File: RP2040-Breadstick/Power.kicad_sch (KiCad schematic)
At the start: 19 parts, among them J501 Conn_01x01, J502 Conn_01x01, J503 Conn_01x01, J504 Conn_01x01, J505 Conn_01x01, J506 Conn_01x01, J507 Conn_01x01, J508 Conn_01x01, J509 Conn_01x01, J510 Conn_01x01, U501 MIC5528-3.3YMT-TR

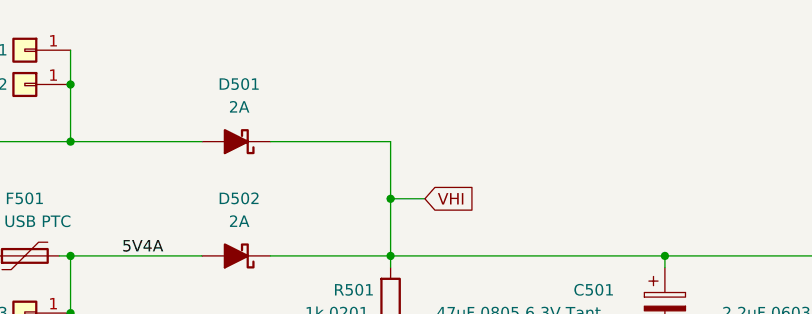
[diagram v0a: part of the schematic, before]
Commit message: Added a note about adding ideal ORing diodes IC
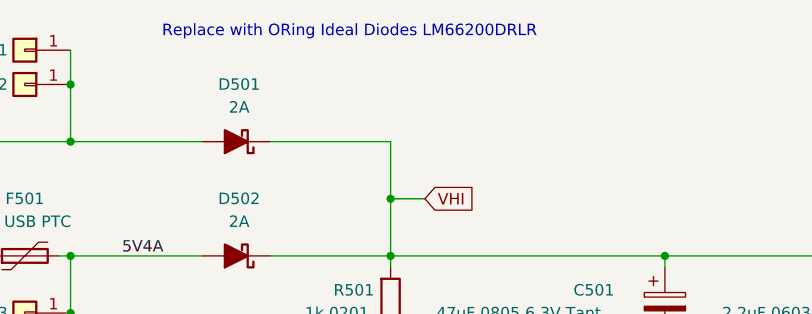
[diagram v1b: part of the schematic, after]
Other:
- note added: "Replace with ORing Ideal Diodes LM66200DRLR"
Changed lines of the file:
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@@
     (stroke (width 0) (type default) (color 0 0 0 0))
+  )
+  (text "Replace with ORing Ideal Diodes LM66200DRLR" (at 74.93 52.07 0)
+    (effects (font (size 1.27 1.27)) (justify left bottom))
   )
   (label "5V4A" (at 70.485 76.2 0)

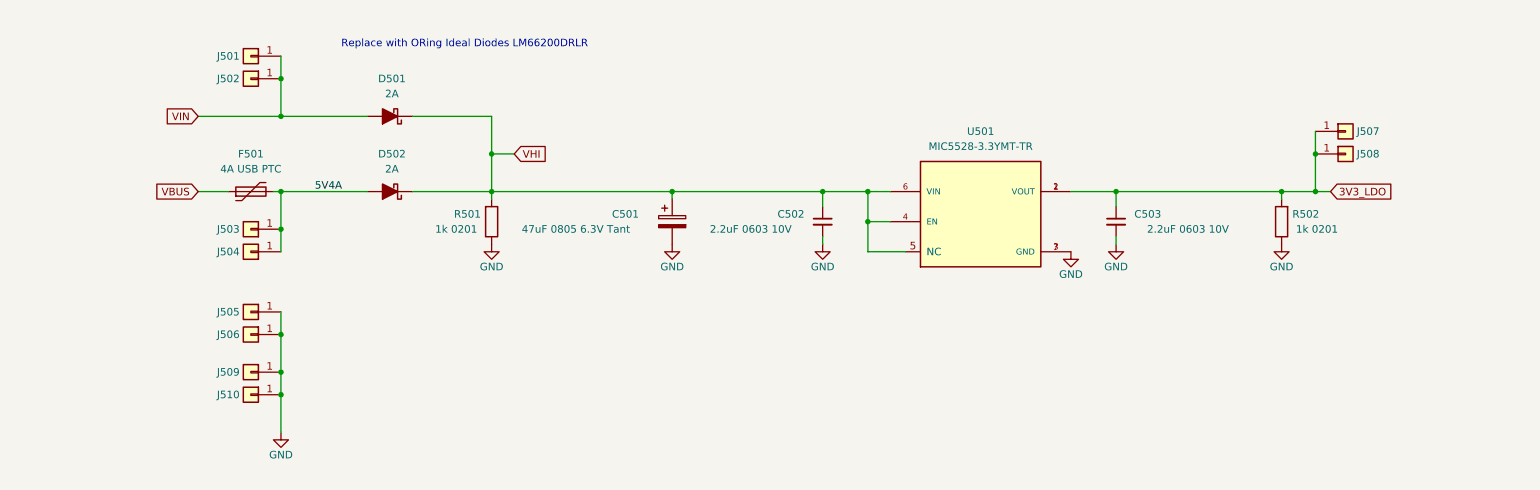
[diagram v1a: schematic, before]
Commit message: Working on several issues simultaneously from the schematic side.
Added hierarchical connections between schematic sheets.
Added ideal ORing diodes.
Unstacked Pins and Added internal diagrams to: USB connector, TVS Diodes, ORing Diodes, LDO, RP2040, etc.
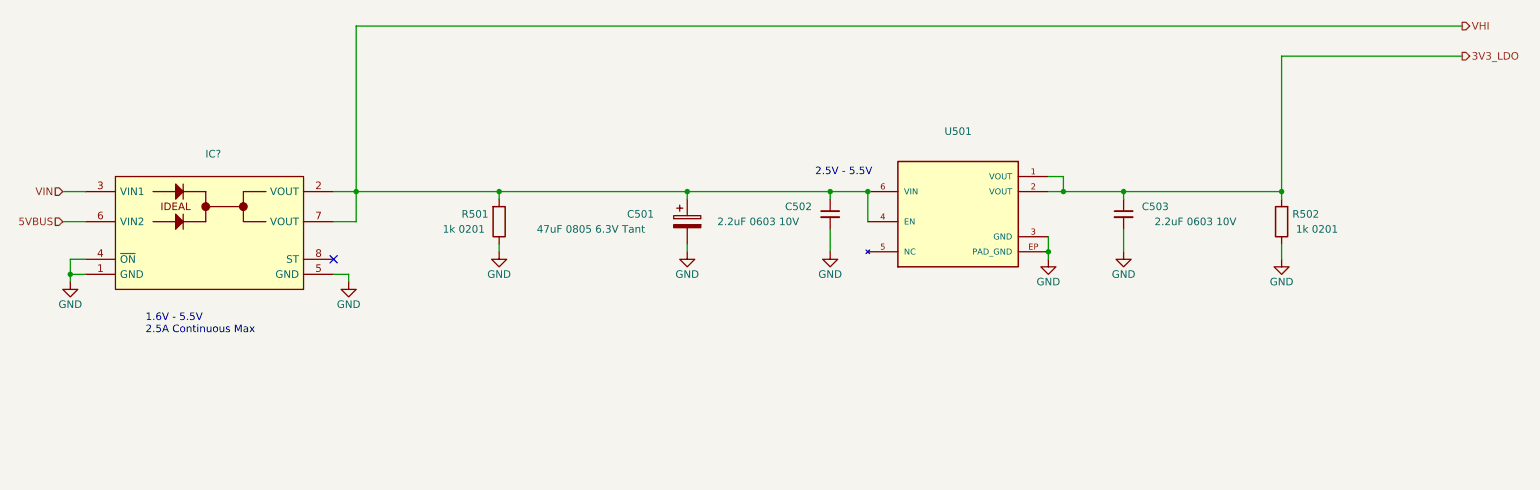
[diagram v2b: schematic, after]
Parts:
- removed D501, D502: 2A, MICROSMP_DO-219AD:DIO_V2PM15HM3_H, symbol Device:D_Schottky_Filled
- removed F501: 4A USB PTC, Fuse:Fuse_0805_2012Metric, symbol Device:Polyfuse
- removed J501, J502, J503, J504, J505, J506, J507, J508, J509, J510: Conn_01x01, Connector_PinHeader_2.54mm:PinHeader_1x01_P2.54mm_Vertical, symbol Connector_Generic:Conn_01x01
- added IC?: (no value), SOTFL50P160X60-8L, symbol LM66200DRLR:LM66200DRLR
- U501: value MIC5528-3.3YMT-TR -> (none); footprint MIC5528-3:SON40P120X120X60-7N -> SON40P120X120X60-7N
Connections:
- net GND: now also U501.EP (PAD_GND), IC?.1 (GND), IC?.4 (~{ON}), IC?.5 (GND); no longer U501.7 (GND)
- net VHI: now also IC?.2 (VOUT), IC?.7 (VOUT); no longer U501.5 (NC)
- net VIN: now also IC?.3 (VIN1)
- new net 5VBUS: IC?.6 (VIN2)
- no-connect marks 0 -> 1
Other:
- note added: "1.6V - 5.5V 2.5A Continuous Max"
- note added: "2.5V - 5.5V"
- note removed: "Replace with ORing Ideal Diodes LM66200DRLR"
- moved on the sheet: C501, C502, C503, R501

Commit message: Moved schematic changes into PCB
All the changes made in the schematic have been moved into the PCB editor. It was a bit of work due to the amount of reorganizing done in the schematic which led to a lot of new reference numbers. Was easy enough to get most things back into place where they were before.
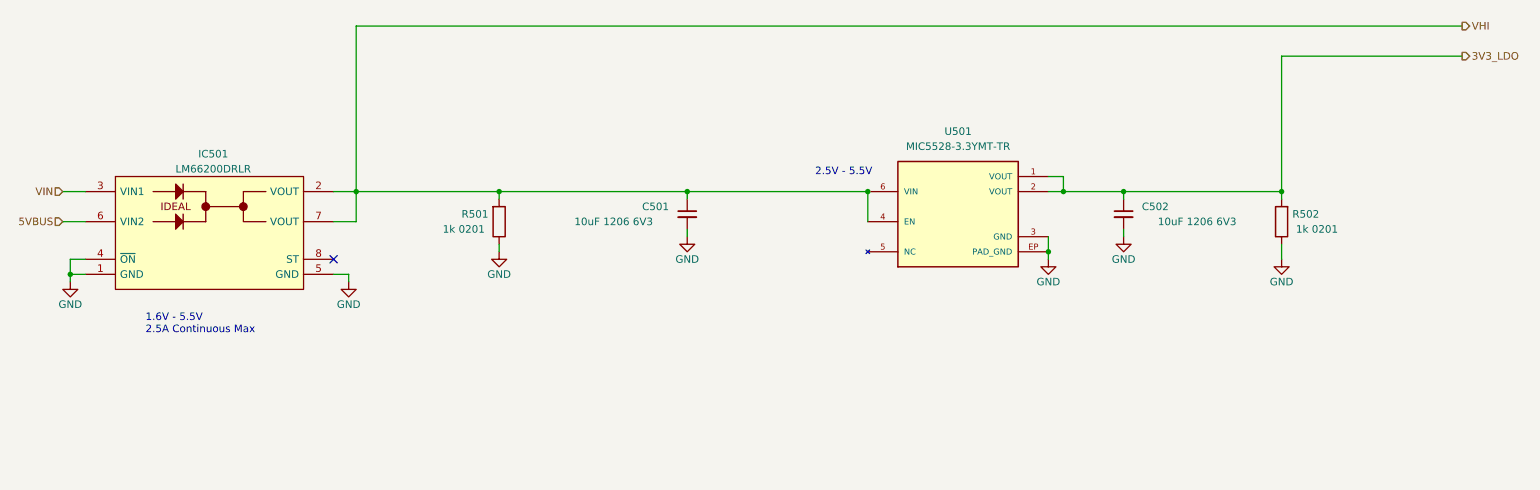
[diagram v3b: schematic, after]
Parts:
- removed C501: 47uF 0805 6.3V Tant, TLJR476M006R3200:CAPC2012X140N, symbol Device:C_Polarized
- removed C503: 2.2uF 0603 10V, Capacitor_SMD:C_0603_1608Metric, symbol Device:C_Small
- added C501: 10uF 1206 6V3, Capacitor_SMD:C_1206_3216Metric, symbol Device:C_Small
- C502: value 2.2uF 0603 10V -> 10uF 1206 6V3; footprint Capacitor_SMD:C_0603_1608Metric -> Capacitor_SMD:C_1206_3216Metric
- IC501: renamed from IC?; value (none) -> LM66200DRLR
- U501: value (none) -> MIC5528-3.3YMT-TR
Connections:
- net 3V3_LDO: now also C502.1
- net GND: now also C501.2
- net VHI: now also C501.1; no longer C502.1
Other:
- title: RP2040 Breadstick -> Raspberry Breadstick

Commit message: Started routing power and LEDs
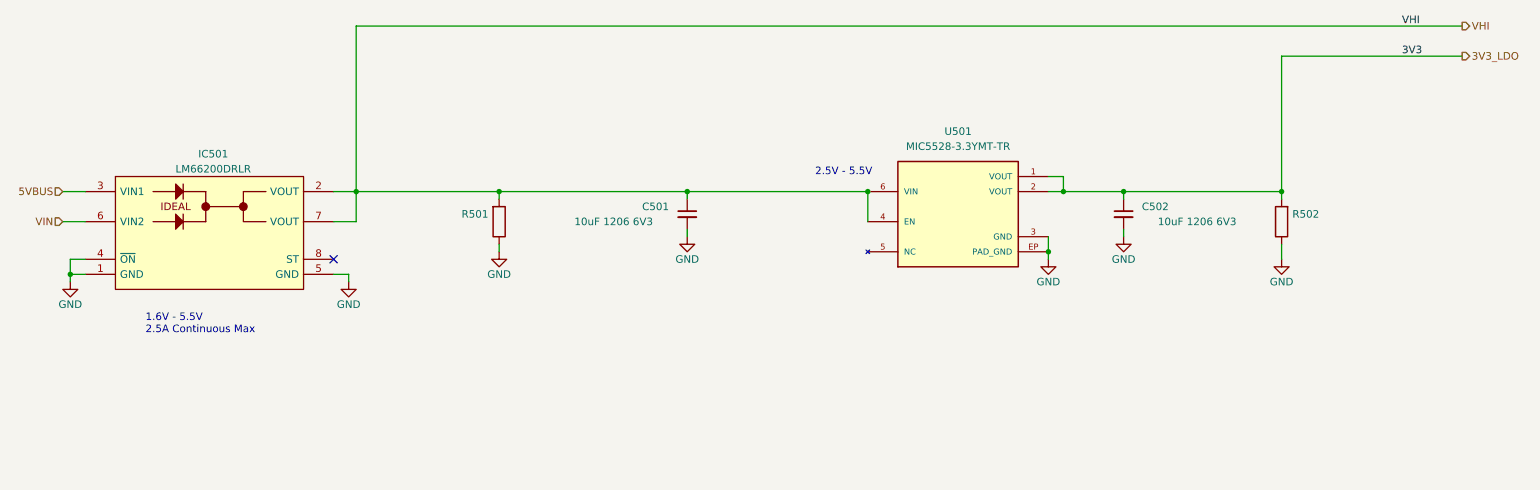
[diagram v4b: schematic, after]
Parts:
- R501, R502: value 1k 0201 -> (none); footprint _Breadstick_Footprints:Perfect_0201_Resistor -> (none)
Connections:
- net 5VBUS: now also IC501.3 (VIN1); no longer IC501.6 (VIN2)
- net VIN: now also IC501.6 (VIN2); no longer IC501.3 (VIN1)
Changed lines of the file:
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@@
+    (stroke (width 0) (type default) (color 0 0 0 0))
+  )
+  (wire (pts (xy 27.94 76.2) (xy 31.75 76.2))
+    (stroke (width 0) (type default) (color 0 0 0 0))
+  )
+  (wire (pts (xy 29.21 90.17) (xy 29.21 91.44))
+    (stroke (width 0) (type default) (color 0 0 0 0))
+  )
+  (wire (pts (xy 194.31 73.66) (xy 196.85 73.66))
+    (stroke (width 0) (type default) (color 0 0 0 0))
+  )
+  (wire (pts (xy 233.68 85.09) (xy 233.68 87.63))
+    (stroke (width 0) (type default) (color 0 0 0 0))
+  )
+  (wire (pts (xy 207.01 76.2) (xy 233.68 76.2))
+    (stroke (width 0) (type default) (color 0 0 0 0))
+  )
+  (wire (pts (xy 194.31 76.2) (xy 196.85 76.2))
+    (stroke (width 0) (type default) (color 0 0 0 0))
+  )
+  (wire (pts (xy 77.47 76.2) (xy 101.6 76.2))
+    (stroke (width 0) (type default) (color 0 0 0 0))
+  )
+  (wire (pts (xy 31.75 87.63) (xy 29.21 87.63))
+    (stroke (width 0) (type default) (color 0 0 0 0))
+  )
+  (wire (pts (xy 196.85 73.66) (xy 196.85 76.2))
+    (stroke (width 0) (type default) (color 0 0 0 0))
+  )
+  (wire (pts (xy 101.6 76.2) (xy 101.6 77.47))
+    (stroke (width 0) (type default) (color 0 0 0 0))
+  )
+  (wire (pts (xy 73.66 90.17) (xy 76.2 90.17))
+    (stroke (width 0) (type default) (color 0 0 0 0))
+  )
+  (wire (pts (xy 233.68 53.34) (xy 233.68 76.2))
+    (stroke (width 0) (type default) (color 0 0 0 0))
+  )
+  (wire (pts (xy 31.75 90.17) (xy 29.21 90.17))
+    (stroke (width 0) (type default) (color 0 0 0 0))
+  )
+  (wire (pts (xy 77.47 48.26) (xy 77.47 76.2))
+    (stroke (width 0) (type default) (color 0 0 0 0))
+  )
+  (wire (pts (xy 77.47 76.2) (xy 77.47 81.28))
+    (stroke (width 0) (type default) (color 0 0 0 0))
+  )
+  (wire (pts (xy 133.35 76.2) (xy 133.35 77.47))
+    (stroke (width 0) (type default) (color 0 0 0 0))
+  )
+  (wire (pts (xy 101.6 76.2) (xy 133.35 76.2))
     (stroke (width 0) (type default) (color 0 0 0 0))
   )
@@
     (stroke (width 0) (type default) (color 0 0 0 0))
   )
-  (wire (pts (xy 29.21 90.17) (xy 29.21 91.44))
-    (stroke (width 0) (type default) (color 0 0 0 0))
-  )
-  (wire (pts (xy 194.31 73.66) (xy 196.85 73.66))
-    (stroke (width 0) (type default) (color 0 0 0 0))
-  )
-  (wire (pts (xy 233.68 85.09) (xy 233.68 87.63))
-    (stroke (width 0) (type default) (color 0 0 0 0))
-  )
-  (wire (pts (xy 207.01 76.2) (xy 233.68 76.2))
-    (stroke (width 0) (type default) (color 0 0 0 0))
-  )
-  (wire (pts (xy 194.31 76.2) (xy 196.85 76.2))
-    (stroke (width 0) (type default) (color 0 0 0 0))
-  )
-  (wire (pts (xy 77.47 76.2) (xy 101.6 76.2))
-    (stroke (width 0) (type default) (color 0 0 0 0))
-  )
-  (wire (pts (xy 31.75 87.63) (xy 29.21 87.63))
-    (stroke (width 0) (type default) (color 0 0 0 0))
-  )
-  (wire (pts (xy 196.85 73.66) (xy 196.85 76.2))
-    (stroke (width 0) (type default) (color 0 0 0 0))
-  )
-  (wire (pts (xy 101.6 76.2) (xy 101.6 77.47))
-    (stroke (width 0) (type default) (color 0 0 0 0))
-  )
-  (wire (pts (xy 73.66 90.17) (xy 76.2 90.17))
-    (stroke (width 0) (type default) (color 0 0 0 0))
-  )
-  (wire (pts (xy 233.68 53.34) (xy 233.68 76.2))
-    (stroke (width 0) (type default) (color 0 0 0 0))
-  )
-  (wire (pts (xy 31.75 90.17) (xy 29.21 90.17))
-    (stroke (width 0) (type default) (color 0 0 0 0))
-  )
-  (wire (pts (xy 77.47 48.26) (xy 77.47 76.2))
-    (stroke (width 0) (type default) (color 0 0 0 0))
-  )
-  (wire (pts (xy 77.47 76.2) (xy 77.47 81.28))
-    (stroke (width 0) (type default) (color 0 0 0 0))
-  )
-  (wire (pts (xy 133.35 76.2) (xy 133.35 77.47))
-    (stroke (width 0) (type default) (color 0 0 0 0))
-  )
-  (wire (pts (xy 101.6 76.2) (xy 133.35 76.2))
-    (stroke (width 0) (type default) (color 0 0 0 0))
-  )
-  (wire (pts (xy 27.94 76.2) (xy 31.75 76.2))
-    (stroke (width 0) (type default) (color 0 0 0 0))
-  )
   (wire (pts (xy 101.6 85.09) (xy 101.6 86.36))
     (stroke (width 0) (type default) (color 0 0 0 0))
@@
   )
   (text "2.5V - 5.5V\n" (at 154.94 73.66 0)
+    (effects (font (size 1.27 1.27)) (justify left bottom))
+  )
+  (label "3V3" (at 254 53.34 0)
+    (effects (font (size 1.27 1.27)) (justify left bottom))
+  )
+  (label "VHI" (at 254 48.26 0)
     (effects (font (size 1.27 1.27)) (justify left bottom))
   )
@@
     (effects (font (size 1.27 1.27)) (justify left))
   )
-  (hierarchical_label "5VBUS" (shape input) (at 27.94 81.28 180)
+  (hierarchical_label "5VBUS" (shape input) (at 27.94 76.2 180)
     (effects (font (size 1.27 1.27)) (justify right))
   )
-  (hierarchical_label "VIN" (shape input) (at 27.94 76.2 180)
+  (hierarchical_label "VIN" (shape input) (at 27.94 81.28 180)
     (effects (font (size 1.27 1.27)) (justify right))
   )
@@
       (effects (font (size 1.27 1.27)) (justify left))
     )
-    (property "Value" "1k 0201" (id 1) (at 243.205 82.55 0)
-      (effects (font (size 1.27 1.27)) (justify left))
-    )
-    (property "Footprint" "_Breadstick_Footprints:Perfect_0201_Resistor" (id 2) (at 235.458 81.28 90)
+    (property "Value" "" (id 1) (at 243.205 82.55 0)
+      (effects (font (size 1.27 1.27)) (justify left))
+    )
+    (property "Footprint" "" (id 2) (at 235.458 81.28 90)
       (effects (font (size 1.27 1.27)) hide)
     )
@@
       (effects (font (size 1.27 1.27)) (justify left))
     )
-    (property "Value" "1k 0201" (id 1) (at 92.075 82.55 0)
-      (effects (font (size 1.27 1.27)) (justify left))
-    )
-    (property "Footprint" "_Breadstick_Footprints:Perfect_0201_Resistor" (id 2) (at 99.822 81.28 90)
-      (effects (font (size 1.27 1.27)) hide)
-    )
+    (property "Value" "" (id 1) (at 92.075 82.55 0)
+      (effects (font (size 1.27 1.27)) (justify left))
+    )
+    (property "Footprint" "" (id 2) (at 99.822 81.28 90)
+      (effects (font (size 1.27 1.27)) hide)
+    )

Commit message: working on rev0.2 still
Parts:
- R501, R502: value (none) -> 1k 0603; footprint (none) -> Resistor_SMD:R_0603_1608Metric
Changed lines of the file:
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@@
       (effects (font (size 1.27 1.27)) (justify left))
     )
-    (property "Value" "" (id 1) (at 243.205 82.55 0)
+    (property "Value" "1k 0603" (id 1) (at 243.205 82.55 0)
       (effects (font (size 1.27 1.27)) (justify left))
     )
-    (property "Footprint" "" (id 2) (at 235.458 81.28 90)
+    (property "Footprint" "Resistor_SMD:R_0603_1608Metric" (id 2) (at 235.458 81.28 90)
       (effects (font (size 1.27 1.27)) hide)
     )
@@
       (effects (font (size 1.27 1.27)) (justify left))
     )
-    (property "Value" "" (id 1) (at 92.075 82.55 0)
+    (property "Value" "1k 0603" (id 1) (at 92.075 82.55 0)
       (effects (font (size 1.27 1.27)) (justify left))
     )
-    (property "Footprint" "" (id 2) (at 99.822 81.28 90)
+    (property "Footprint" "Resistor_SMD:R_0603_1608Metric" (id 2) (at 99.822 81.28 90)
       (effects (font (size 1.27 1.27)) hide)
     )

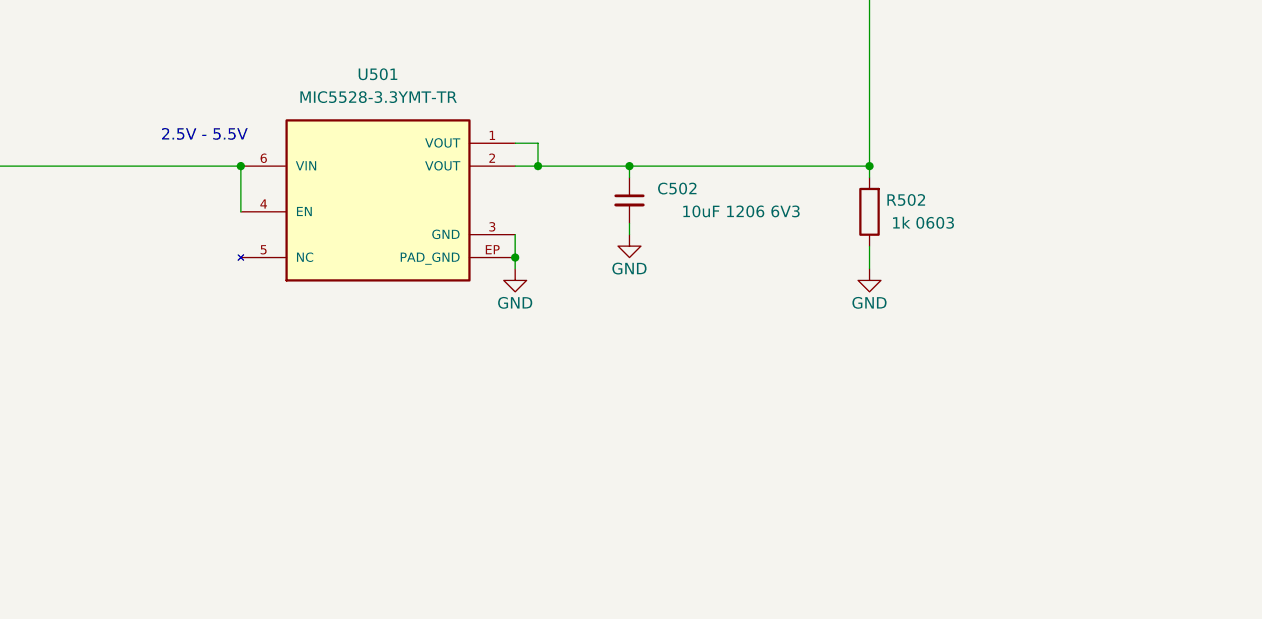
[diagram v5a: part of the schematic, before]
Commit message: Moved All Parts to Top
Exploring how this can be done with the largest components possible, all on the top side of the board.
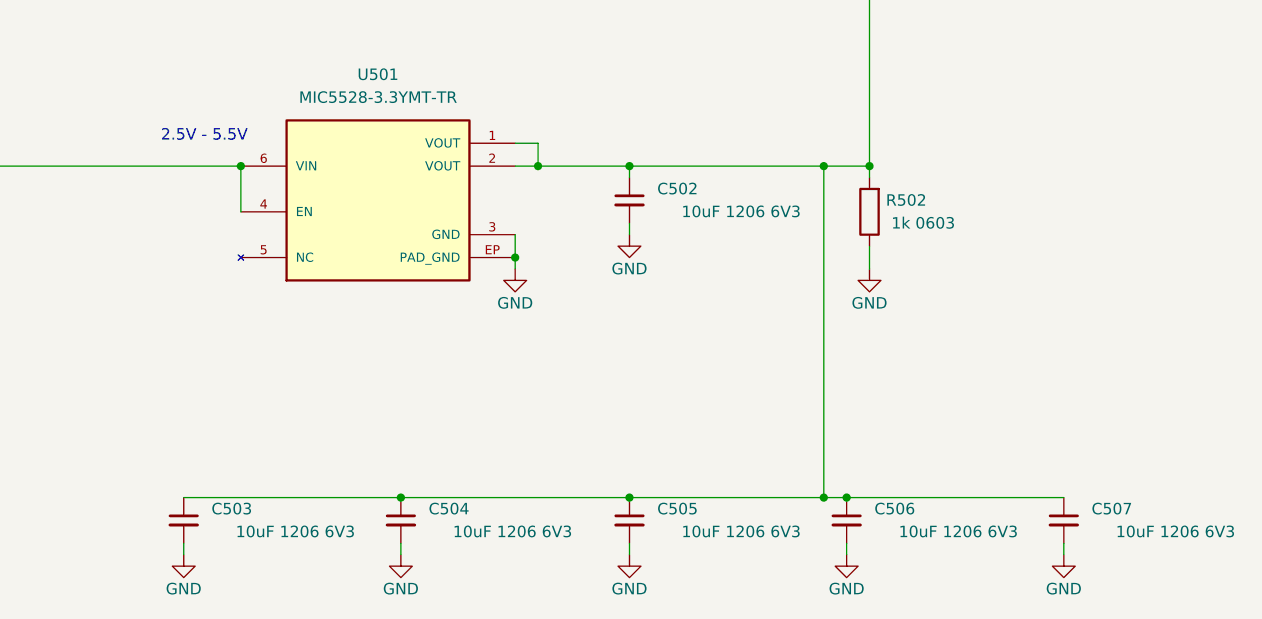
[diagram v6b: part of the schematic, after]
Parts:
- added C503, C504, C505, C506, C507: 10uF 1206 6V3, Capacitor_SMD:C_1206_3216Metric, symbol Device:C_Small
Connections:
- net 3V3_LDO: now also C503.1, C504.1, C505.1, C506.1, C507.1
- net GND: now also C503.2, C504.2, C505.2, C506.2, C507.2
